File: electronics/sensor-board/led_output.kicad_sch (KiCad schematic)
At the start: 12 parts, among them J19 Conn_02x04_Odd_Even, U11 74HCT245

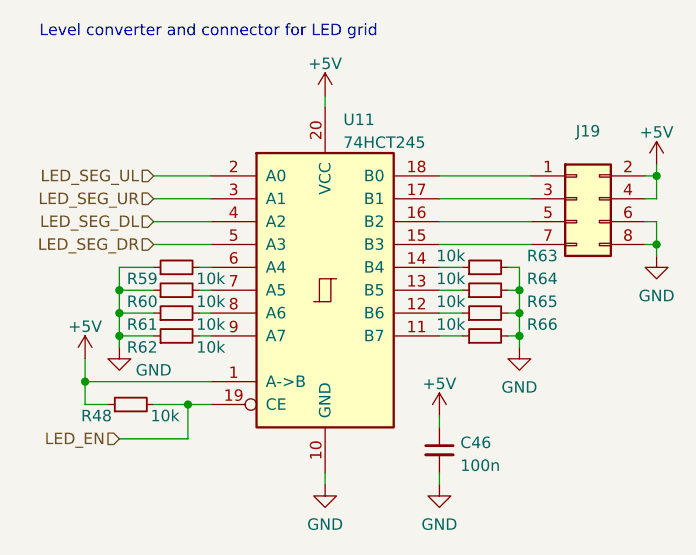
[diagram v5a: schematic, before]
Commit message: Update reference designators
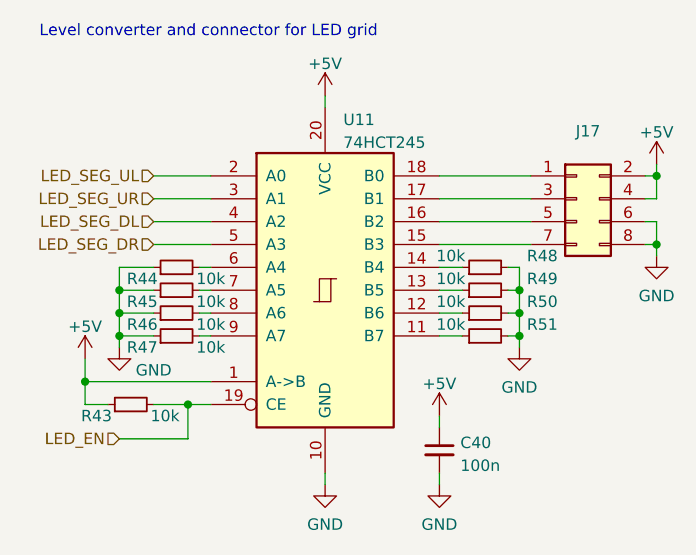
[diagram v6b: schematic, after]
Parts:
- renumbered C46 to C40, J19 to J17, R48 to R43, R59 to R44, R60 to R45, R61 to R46, R62 to R47, R63 to R48, R64 to R49, R65 to R50, R66 to R51
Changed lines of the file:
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@@
   (symbol (lib_id "Device:R_Small") (at 36.83 41.91 90) (unit 1)
     (in_bom yes) (on_board yes)
-    (property "Reference" "R59" (id 0) (at 33.02 43.18 90))
+    (property "Reference" "R44" (id 0) (at 33.02 43.18 90))
     (property "Value" "10k" (id 1) (at 40.64 43.18 90))
     (property "Footprint" "Resistor_SMD:R_0603_1608Metric" (id 2) (at 36.83 41.91 0)
@@
   (symbol (lib_id "Device:R_Small") (at 71.12 41.91 90) (unit 1)
     (in_bom yes) (on_board yes)
-    (property "Reference" "R63" (id 0) (at 77.47 40.64 90))
+    (property "Reference" "R48" (id 0) (at 77.47 40.64 90))
     (property "Value" "10k" (id 1) (at 67.31 40.64 90))
     (property "Footprint" "Resistor_SMD:R_0603_1608Metric" (id 2) (at 71.12 41.91 0)
@@
   (symbol (lib_id "power:GND") (at 53.34 66.04 0) (unit 1)
     (in_bom yes) (on_board yes) (fields_autoplaced)
-    (property "Reference" "#PWR0108" (id 0) (at 53.34 72.39 0)
+    (property "Reference" "#PWR099" (id 0) (at 53.34 72.39 0)
       (effects (font (size 1.27 1.27)) hide)
     )
@@
   (symbol (lib_id "power:GND") (at 66.04 66.04 0) (unit 1)
     (in_bom yes) (on_board yes) (fields_autoplaced)
-    (property "Reference" "#PWR0110" (id 0) (at 66.04 72.39 0)
+    (property "Reference" "#PWR0101" (id 0) (at 66.04 72.39 0)
       (effects (font (size 1.27 1.27)) hide)
     )
@@
   (symbol (lib_id "Device:R_Small") (at 71.12 46.99 90) (unit 1)
     (in_bom yes) (on_board yes)
-    (property "Reference" "R65" (id 0) (at 77.47 45.72 90))
+    (property "Reference" "R50" (id 0) (at 77.47 45.72 90))
     (property "Value" "10k" (id 1) (at 67.31 45.72 90))
     (property "Footprint" "Resistor_SMD:R_0603_1608Metric" (id 2) (at 71.12 46.99 0)
@@
   (symbol (lib_id "power:GND") (at 30.48 50.8 0) (unit 1)
     (in_bom yes) (on_board yes)
-    (property "Reference" "#PWR0105" (id 0) (at 30.48 57.15 0)
+    (property "Reference" "#PWR097" (id 0) (at 30.48 57.15 0)
       (effects (font (size 1.27 1.27)) hide)
     )
@@
   (symbol (lib_id "power:+5V") (at 66.04 58.42 0) (unit 1)
     (in_bom yes) (on_board yes) (fields_autoplaced)
-    (property "Reference" "#PWR0109" (id 0) (at 66.04 62.23 0)
+    (property "Reference" "#PWR0100" (id 0) (at 66.04 62.23 0)
       (effects (font (size 1.27 1.27)) hide)
     )
@@
   (symbol (lib_id "power:GND") (at 74.93 50.8 0) (unit 1)
     (in_bom yes) (on_board yes) (fields_autoplaced)
-    (property "Reference" "#PWR0111" (id 0) (at 74.93 57.15 0)
+    (property "Reference" "#PWR0102" (id 0) (at 74.93 57.15 0)
       (effects (font (size 1.27 1.27)) hide)
     )
@@
   (symbol (lib_id "power:+5V") (at 26.67 52.07 0) (unit 1)
     (in_bom yes) (on_board yes) (fields_autoplaced)
-    (property "Reference" "#PWR0104" (id 0) (at 26.67 55.88 0)
+    (property "Reference" "#PWR096" (id 0) (at 26.67 55.88 0)
       (effects (font (size 1.27 1.27)) hide)
     )
@@
   (symbol (lib_id "Device:R_Small") (at 71.12 44.45 90) (unit 1)
     (in_bom yes) (on_board yes)
-    (property "Reference" "R64" (id 0) (at 77.47 43.18 90))
+    (property "Reference" "R49" (id 0) (at 77.47 43.18 90))
     (property "Value" "10k" (id 1) (at 67.31 43.18 90))
     (property "Footprint" "Resistor_SMD:R_0603_1608Metric" (id 2) (at 71.12 44.45 0)
@@
   (symbol (lib_id "Device:R_Small") (at 36.83 49.53 90) (unit 1)
     (in_bom yes) (on_board yes)
-    (property "Reference" "R62" (id 0) (at 33.02 50.8 90))
+    (property "Reference" "R47" (id 0) (at 33.02 50.8 90))
     (property "Value" "10k" (id 1) (at 40.64 50.8 90))
     (property "Footprint" "Resistor_SMD:R_0603_1608Metric" (id 2) (at 36.83 49.53 0)
@@
   (symbol (lib_id "power:GND") (at 90.17 40.64 0) (unit 1)
     (in_bom yes) (on_board yes) (fields_autoplaced)
-    (property "Reference" "#PWR0113" (id 0) (at 90.17 46.99 0)
+    (property "Reference" "#PWR0104" (id 0) (at 90.17 46.99 0)
       (effects (font (size 1.27 1.27)) hide)
     )
@@
   (symbol (lib_id "power:+5V") (at 53.34 22.86 0) (unit 1)
     (in_bom yes) (on_board yes) (fields_autoplaced)
-    (property "Reference" "#PWR0107" (id 0) (at 53.34 26.67 0)
+    (property "Reference" "#PWR098" (id 0) (at 53.34 26.67 0)
       (effects (font (size 1.27 1.27)) hide)
     )
@@
   (symbol (lib_id "Device:R_Small") (at 36.83 46.99 90) (unit 1)
     (in_bom yes) (on_board yes)
-    (property "Reference" "R61" (id 0) (at 33.02 48.26 90))
+    (property "Reference" "R46" (id 0) (at 33.02 48.26 90))
     (property "Value" "10k" (id 1) (at 40.64 48.26 90))
     (property "Footprint" "Resistor_SMD:R_0603_1608Metric" (id 2) (at 36.83 46.99 0)
@@
   (symbol (lib_id "Device:R_Small") (at 31.75 57.15 90) (unit 1)
     (in_bom yes) (on_board yes)
-    (property "Reference" "R48" (id 0) (at 27.94 58.42 90))
+    (property "Reference" "R43" (id 0) (at 27.94 58.42 90))
     (property "Value" "10k" (id 1) (at 35.56 58.42 90))
     (property "Footprint" "Resistor_SMD:R_0603_1608Metric" (id 2) (at 31.75 57.15 0)
@@
   (symbol (lib_id "Device:R_Small") (at 71.12 49.53 90) (unit 1)
     (in_bom yes) (on_board yes)
-    (property "Reference" "R66" (id 0) (at 77.47 48.26 90))
+    (property "Reference" "R51" (id 0) (at 77.47 48.26 90))
     (property "Value" "10k" (id 1) (at 67.31 48.26 90))
     (property "Footprint" "Resistor_SMD:R_0603_1608Metric" (id 2) (at 71.12 49.53 0)
@@
   (symbol (lib_id "Connector_Generic:Conn_02x04_Odd_Even") (at 81.28 34.29 0) (unit 1)
     (in_bom yes) (on_board yes) (fields_autoplaced)
-    (property "Reference" "J19" (id 0) (at 82.55 26.7802 0))
+    (property "Reference" "J17" (id 0) (at 82.55 26.7802 0))
     (property "Value" "Conn_02x04_Odd_Even" (id 1) (at 82.55 29.3171 0)
       (effects (font (size 1.27 1.27)) hide)
@@
   (symbol (lib_id "Device:C_Small") (at 66.04 62.23 0) (unit 1)
     (in_bom yes) (on_board yes) (fields_autoplaced)
-    (property "Reference" "C46" (id 0) (at 68.3641 61.4016 0)
+    (property "Reference" "C40" (id 0) (at 68.3641 61.4016 0)
       (effects (font (size 1.27 1.27)) (justify left))
     )
@@
   (symbol (lib_id "Device:R_Small") (at 36.83 44.45 90) (unit 1)
     (in_bom yes) (on_board yes)
-    (property "Reference" "R60" (id 0) (at 33.02 45.72 90))
+    (property "Reference" "R45" (id 0) (at 33.02 45.72 90))
     (property "Value" "10k" (id 1) (at 40.64 45.72 90))
     (property "Footprint" "Resistor_SMD:R_0603_1608Metric" (id 2) (at 36.83 44.45 0)
@@
   (symbol (lib_id "power:+5V") (at 90.17 30.48 0) (unit 1)
     (in_bom yes) (on_board yes) (fields_autoplaced)
-    (property "Reference" "#PWR0112" (id 0) (at 90.17 34.29 0)
-      (effects (font (size 1.27 1.27)) hide)
-    )
+    (property "Reference" "#PWR0103" (id 0) (at 90.17 34.29 0)
+      (effects (font (size 1.27 1.27)) hide)
+    )

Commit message: Switch to G4, preliminary signal layout
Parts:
- J17: footprint Connector_PinHeader_2.54mm:PinHeader_2x04_P2.54mm_Vertical -> Connector_IDC:IDC-Header_2x04_P2.54mm_Vertical
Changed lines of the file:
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@@
       (effects (font (size 1.27 1.27)) hide)
     )
-    (property "Footprint" "Connector_PinHeader_2.54mm:PinHeader_2x04_P2.54mm_Vertical" (id 2) (at 81.28 34.29 0)
+    (property "Footprint" "Connector_IDC:IDC-Header_2x04_P2.54mm_Vertical" (id 2) (at 81.28 34.29 0)
       (effects (font (size 1.27 1.27)) hide)
     )
